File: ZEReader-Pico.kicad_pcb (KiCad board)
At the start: 2 copper layers, 110 x 110 mm, 77 parts, among them J1 Micro_SD_Card_Det2, J2 UART, J3 SWD, J4 Conn_01x24_MountingPin, J5 2171790001, J6 Conn_01x02_Socket, Q1 Si1308EDL, Q2 DMG2305UX-7, SW1 SW_Push, SW2 SW_Push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

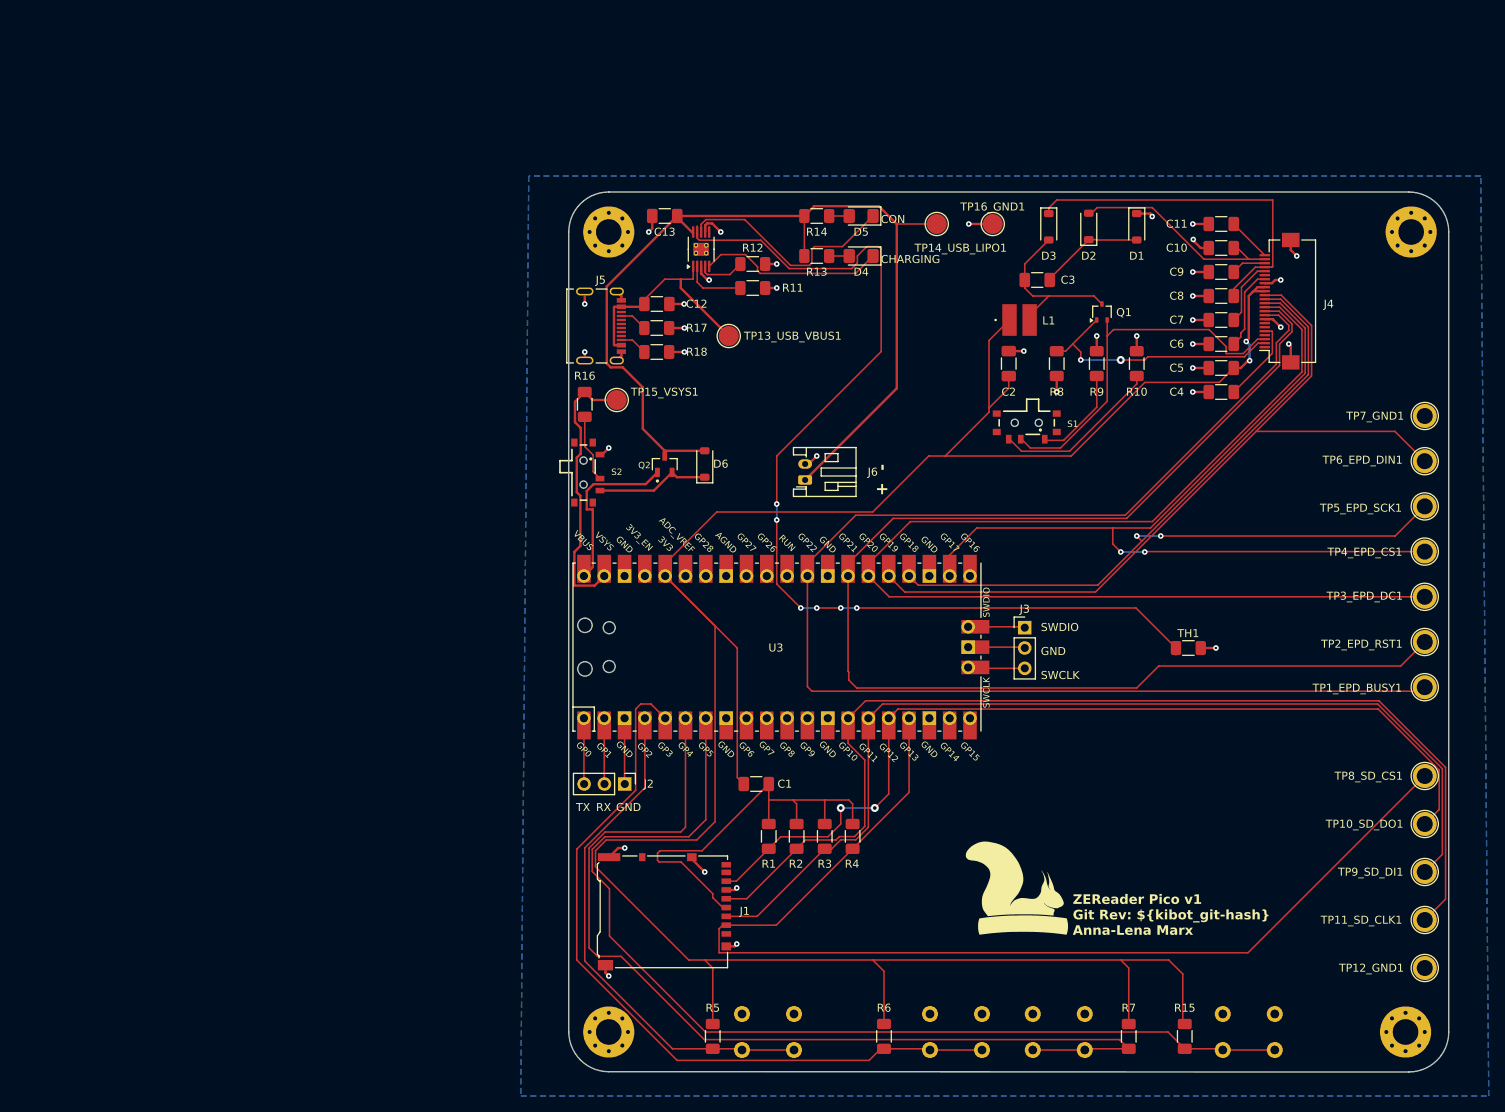
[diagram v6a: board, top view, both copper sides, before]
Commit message: fix: corrected button/connector location
Signed-off-by: Anna-Lena Marx <anna-lena.marx@web.de>
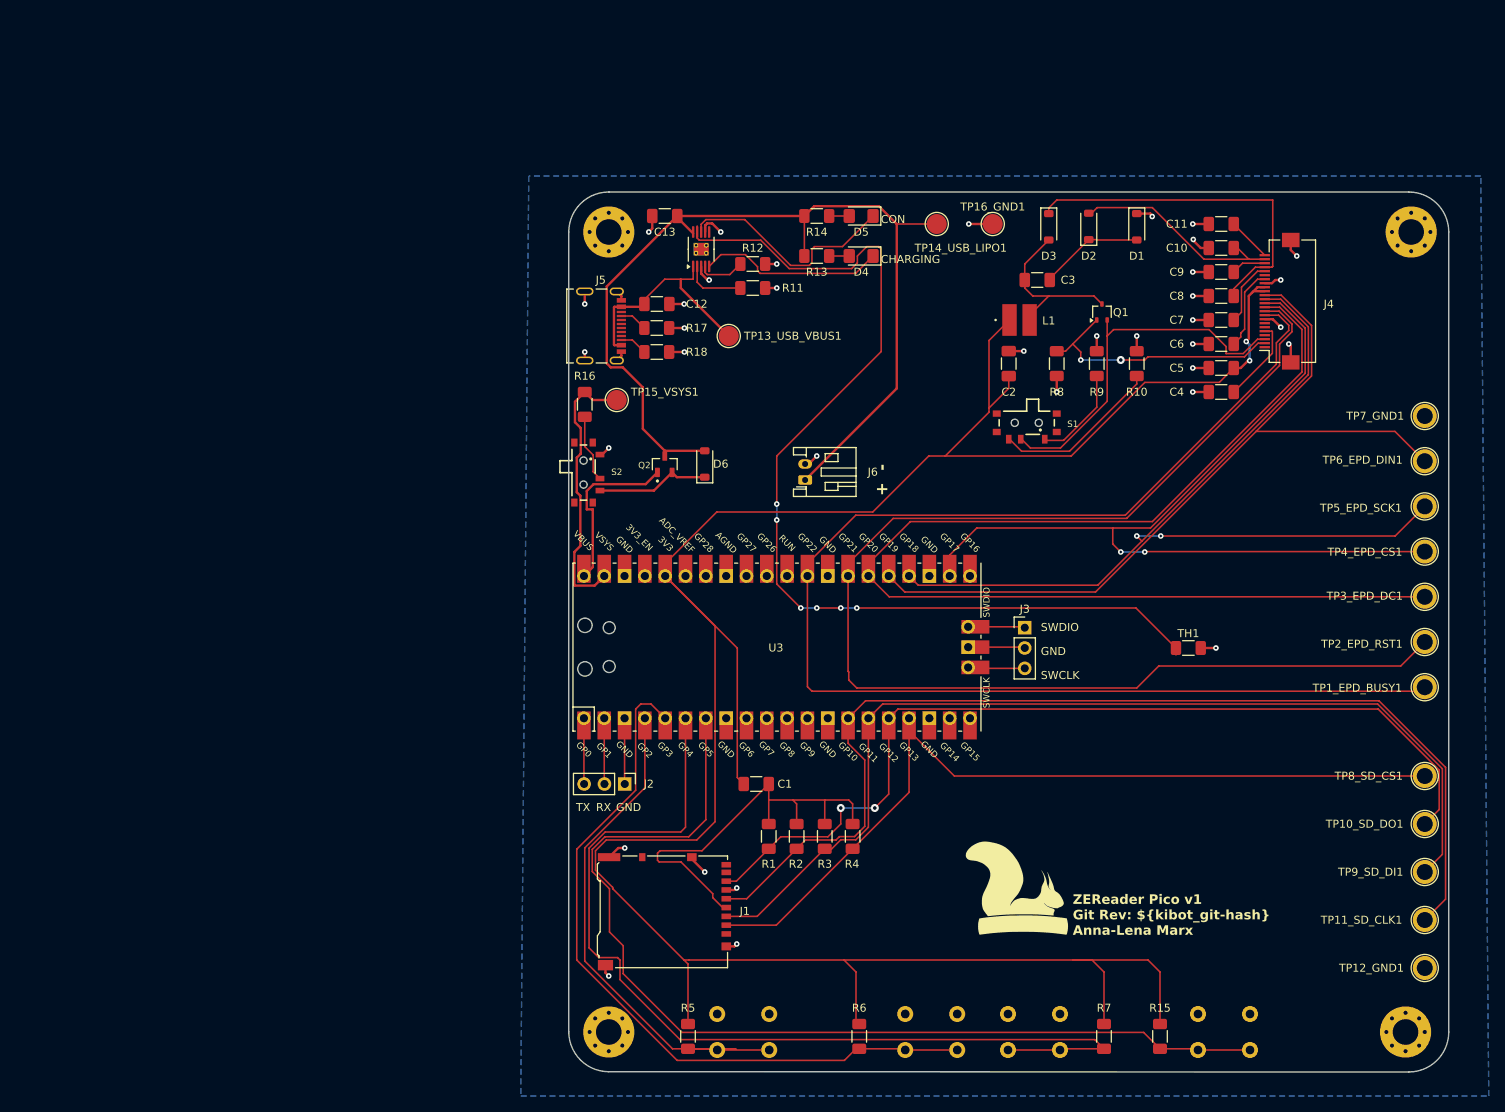
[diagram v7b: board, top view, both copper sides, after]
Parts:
- moved R15 3.09 mm to (174.0, 145.6)
- moved R5 3.09 mm to (115.0, 145.6)
- moved R6 3.09 mm to (136.4, 145.6)
- moved R7 3.09 mm to (167.0, 145.6)
- moved SW1 3.09 mm to (125.2, 142.8)
- moved SW2 3.09 mm to (148.7, 142.8)
- moved SW3 3.09 mm to (161.5, 142.8)
- moved SW4 3.09 mm to (185.2, 142.8)
- moved G*** 0.78 mm to (194.5, 144.5)
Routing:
- net SD_DAT3-CD-CS: track 140.4 -> 107.8 mm
- net BTN_2: track 95.2 -> 92.1 mm
- net BTN_1: track 64.3 -> 67.2 mm
- net BTN_3: track 124.0 -> 122.4 mm
- net +3.3V: track 314.4 -> 315.7 mm
- net BTN_4: track 129.2 -> 127.9 mm

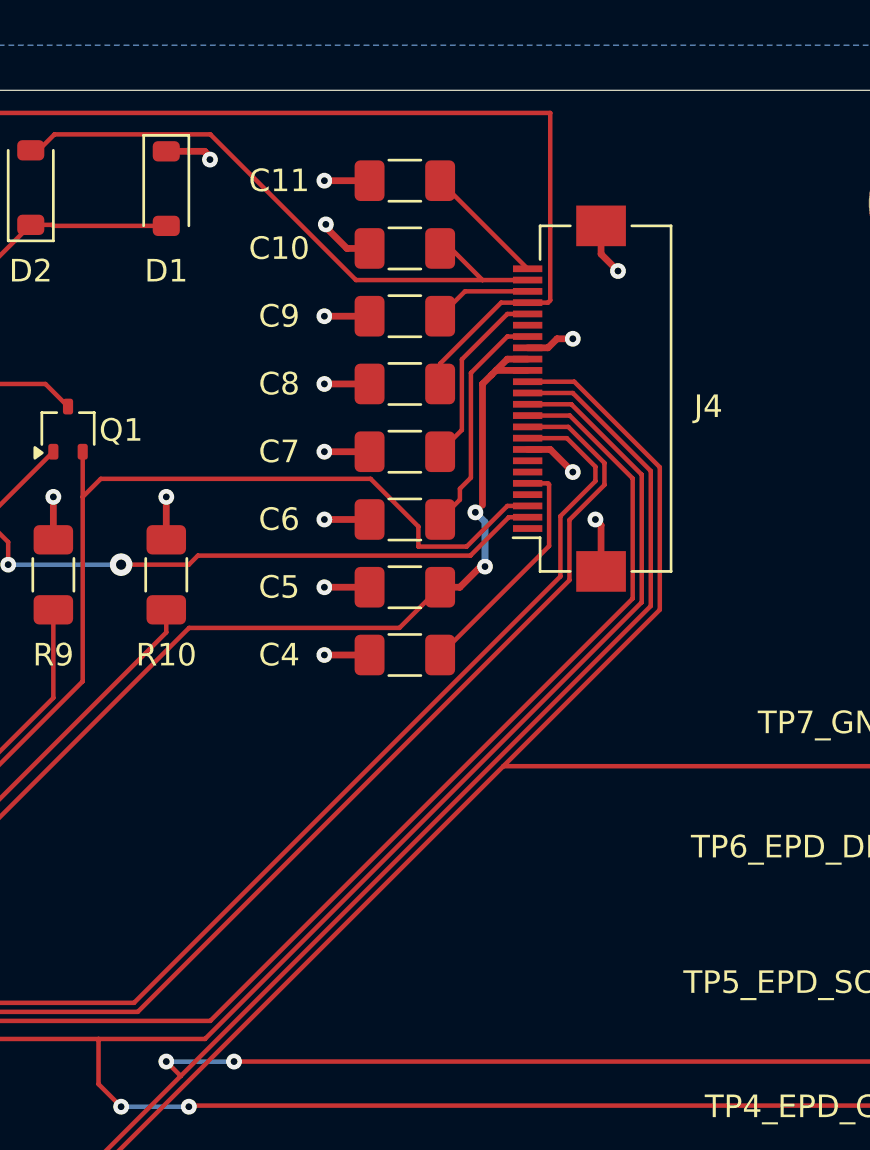
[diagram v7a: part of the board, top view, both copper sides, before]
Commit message: try alternate display connector
Signed-off-by: Anna-Lena Marx <anna-lena.marx@web.de>
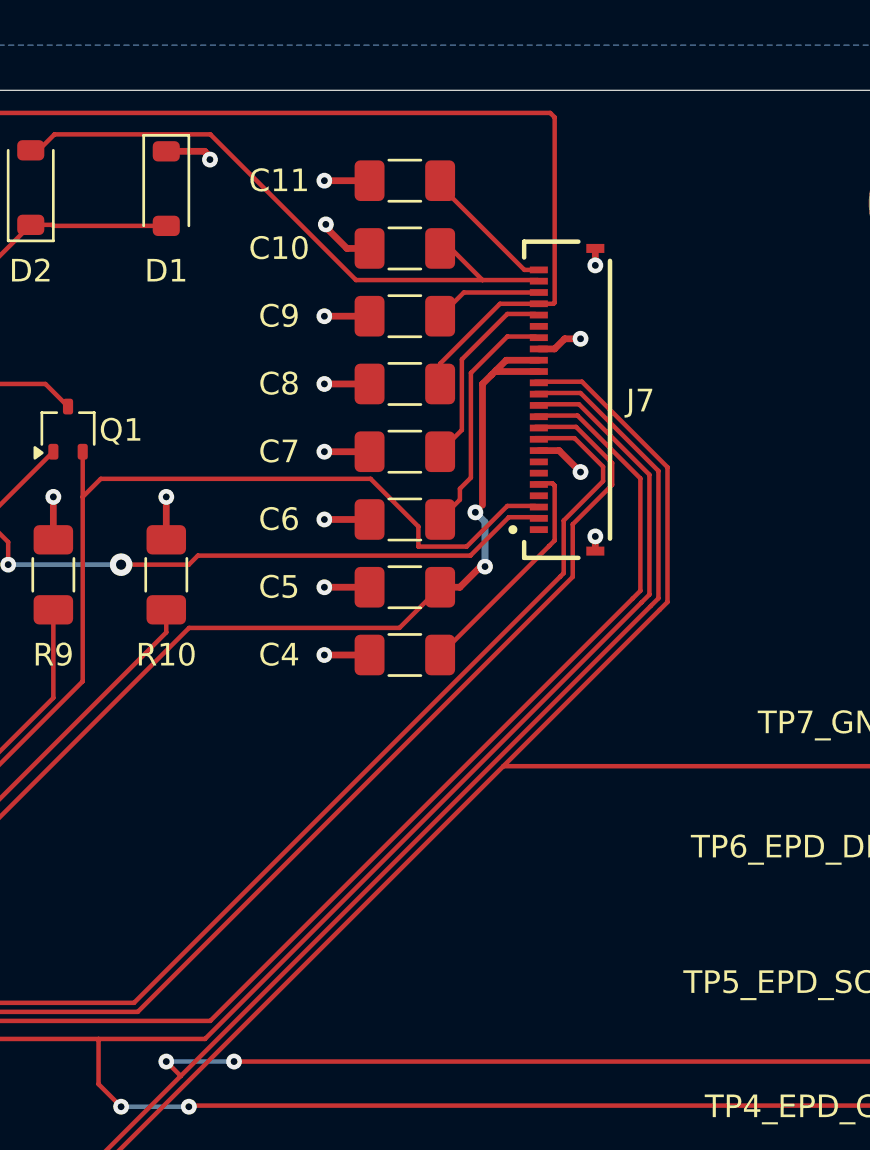
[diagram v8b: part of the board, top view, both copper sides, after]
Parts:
- removed J4: Conn_01x24_MountingPin, Connector_FFC-FPC:Hirose_FH12-24S-0.5SH_1x24-1MP_P0.50mm_Horizontal
- added J7: FFC2B28-24-G, prj-footprints:GCT_FFC2B28-24-G, F.Cu at (188.8, 53.7)
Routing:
- net GND: track 90.2 -> 86.6 mm
- net +3.3V: track 315.7 -> 316.7 mm
- net Net-(C11-Pad2): track 5.51 -> 6.14 mm
- net /03_ePaper-Driver/VGL: track 27.4 -> 27.9 mm
